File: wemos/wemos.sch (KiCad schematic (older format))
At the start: 5 parts, among them SW1 SW_SPST, U1 wemos

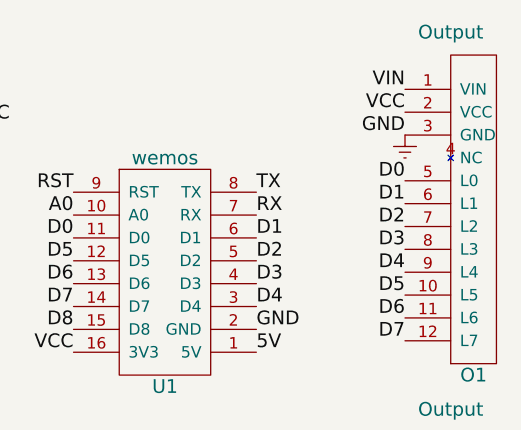
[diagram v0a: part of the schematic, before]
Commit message: More update to make the libraryies use only relative paths.
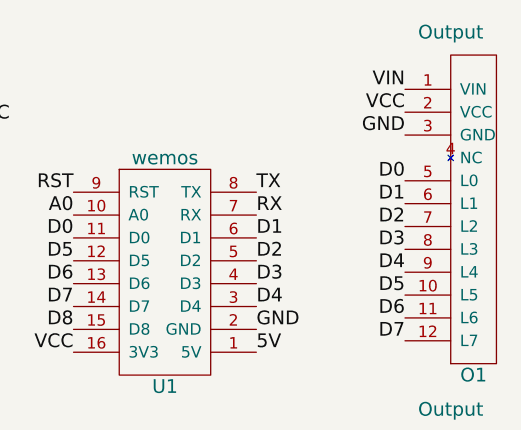
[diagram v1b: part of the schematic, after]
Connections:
- net Earth renamed GND
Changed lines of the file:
@@
 LIBS:valves
 LIBS:eplay
-LIBS:wemos-cache
 EELAYER 25 0
 EELAYER END
@@
 VIN
 $Comp
-L Earth #PWR01
-U 1 1 5AC24527
-P 6000 2050
-F 0 "#PWR01" H 6000 1800 50  0001 C CNN
-F 1 "Earth" H 6000 1900 50  0001 C CNN
-F 2 "" H 6000 2050 50  0001 C CNN
-F 3 "" H 6000 2050 50  0001 C CNN
-	1    6000 2050
-	1    0    0    -1
-$EndComp
-$Comp
 L Output O1
